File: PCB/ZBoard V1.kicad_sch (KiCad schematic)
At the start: 174 parts, among them SW1 SW_Push, SW10 SW_Push, SW11 SW_Push, SW12 SW_Push, SW13 SW_Push, SW14 SW_Push, SW15 SW_Push, SW16 SW_Push, SW17 SW_Push, SW18 SW_Push, SW19 SW_Push, SW2 SW_Push, SW20 SW_Push, SW21 SW_Push, SW22 SW_Push, SW23 SW_Push, SW24 SW_Push, SW25 SW_Push, SW26 SW_Push, SW27 SW_Push, SW28 SW_Push, SW29 SW_Push, SW3 SW_Push, SW30 SW_Push, SW31 SW_Push, SW32 SW_Push, SW33 SW_Push, SW34 SW_Push, SW35 SW_Push, SW36 SW_Push, SW37 SW_Push, SW38 SW_Push, SW39 SW_Push, SW4 SW_Push, SW40 SW_Push, SW41 SW_Push, SW42 SW_Push, SW43 SW_Push, SW44 SW_Push, SW45 SW_Push, SW46 SW_Push, SW47 SW_Push, SW48 SW_Push, SW49 SW_Push, SW5 SW_Push, SW50 SW_Push, SW51 SW_Push, SW52 SW_Push, SW53 SW_Push, SW54 SW_Push, SW55 SW_Push, SW56 SW_Push, SW57 SW_Push, SW58 SW_Push, SW59 SW_Push, SW6 SW_Push, SW60 SW_Push, SW61 SW_Push, SW62 SW_Push, SW63 SW_Push, SW64 SW_Push, SW65 SW_Push, SW66 SW_Push, SW67 SW_Push, SW68 SW_Push, SW69 SW_Push, SW7 SW_Push, SW70 SW_Push, SW71 SW_Push, SW72 SW_Push, SW73 SW_Push, SW74 SW_Push, SW75 SW_Push, SW76 SW_Push, SW77 SW_Push, SW78 SW_Push, SW79 SW_Push, SW8 SW_Push, SW80 SW_Push, SW81 SW_Push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

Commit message: Fixed pinouts, fixed firmware
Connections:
- net ROW1: now also U1.9 (P1.13_D8_SCK); no longer U1.6 (P0.05_A5_D5_SCL)
- net SCK renamed SCL
- net SCL: now also U1.6 (P0.05_A5_D5_SCL); no longer U1.9 (P1.13_D8_SCK)
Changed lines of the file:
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@@
 		)
 	)
-	(label "SCK"
+	(label "SCL"
 		(at 87.63 177.8 180)
 		(effects
@@
 		)
 	)
-	(label "ROW1"
+	(label "SCL"
 		(at 20.32 203.2 180)
 		(effects
@@
 		)
 	)
-	(label "SCK"
+	(label "ROW1"
 		(at 62.23 203.2 0)
 		(effects

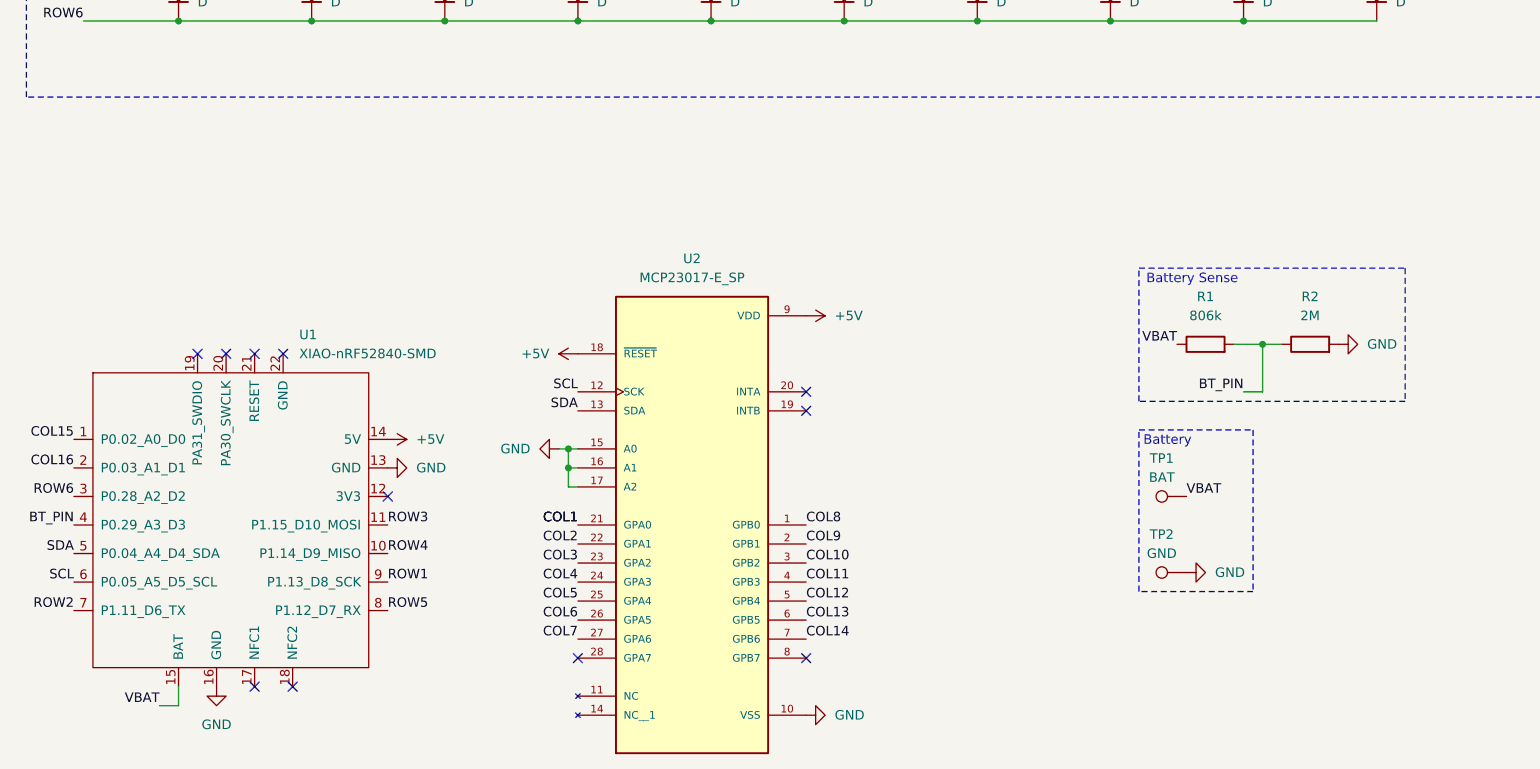
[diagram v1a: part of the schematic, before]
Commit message: Beginning transition to wired using Orpheus Pico
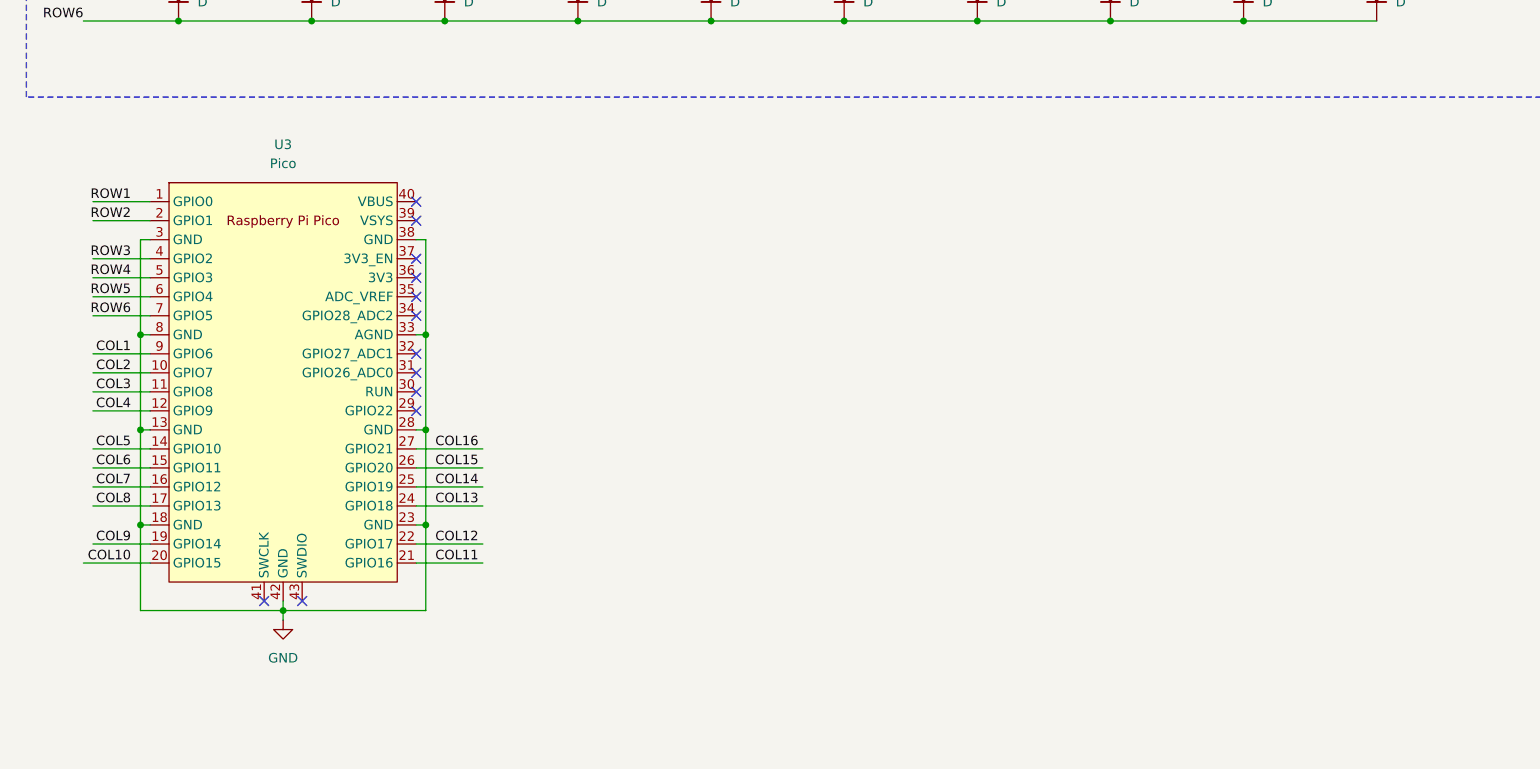
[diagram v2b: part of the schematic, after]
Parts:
- removed R1: 806k, MFR-25FRF52-806k:MFR-25FRF52-806k, symbol Device:R
- removed R2: 2M, MFR-25FRF52-2M:MFR-25FRF52-2M, symbol Device:R
- removed TP1: BAT, TestPoint:TestPoint_Pad_D2.0mm, symbol Connector:TestPoint
- removed TP2: GND, TestPoint:TestPoint_Pad_2.0x2.0mm, symbol Connector:TestPoint
- removed U1: XIAO-nRF52840-SMD, Modified-XIAO:modified-XIAO-nRF52840-SMD, symbol Seeed_Studio_XIAO_Series:XIAO-nRF52840-SMD
- removed U2: MCP23017-E_SP, MCP23017_GPIO:MCP23107_GPIO, symbol MCP23017-E_SP_GPIO:MCP23017-E_SP
- added U3: Pico, MCU_RaspberryPi_and_Boards:RPi_Pico_SMD_TH, symbol MCU_RaspberryPi_and_Boards:Pico
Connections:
- net COL1: now also U3.9 (GPIO6)
- net COL10: now also U3.20 (GPIO15)
- net COL11: now also U3.21 (GPIO16)
- net COL12: now also U3.22 (GPIO17)
- net COL13: now also U3.24 (GPIO18)
- net COL14: now also U3.25 (GPIO19)
- net COL15: now also U3.26 (GPIO20)
- net COL16: now also U3.27 (GPIO21)
- net COL2: now also U3.10 (GPIO7)
- net COL3: now also U3.11 (GPIO8)
- net COL4: now also U3.12 (GPIO9)
- net COL5: now also U3.14 (GPIO10)
- net COL6: now also U3.15 (GPIO11)
- net COL7: now also U3.16 (GPIO12)
- net COL8: now also U3.17 (GPIO13)
- net COL9: now also U3.19 (GPIO14)
- net GND: now also U3.13 (GND), U3.18 (GND), U3.23 (GND), U3.28 (GND), U3.3 (GND), U3.33 (AGND), U3.38 (GND), U3.42 (GND), U3.8 (GND)
- net ROW1: now also U3.1 (GPIO0)
- net ROW2: now also U3.2 (GPIO1)
- net ROW3: now also U3.4 (GPIO2)
- net ROW4: now also U3.5 (GPIO3)
- net ROW5: now also U3.6 (GPIO4)
- net ROW6: now also U3.7 (GPIO5)
- no-connect marks 11 -> 12
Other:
- note removed: "Battery"
- note removed: "Battery Sense"
